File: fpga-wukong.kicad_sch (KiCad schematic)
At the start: 2 parts, among them J4 QMTECH FPGA Module U4, J5 QMTECH FPGA Module U5

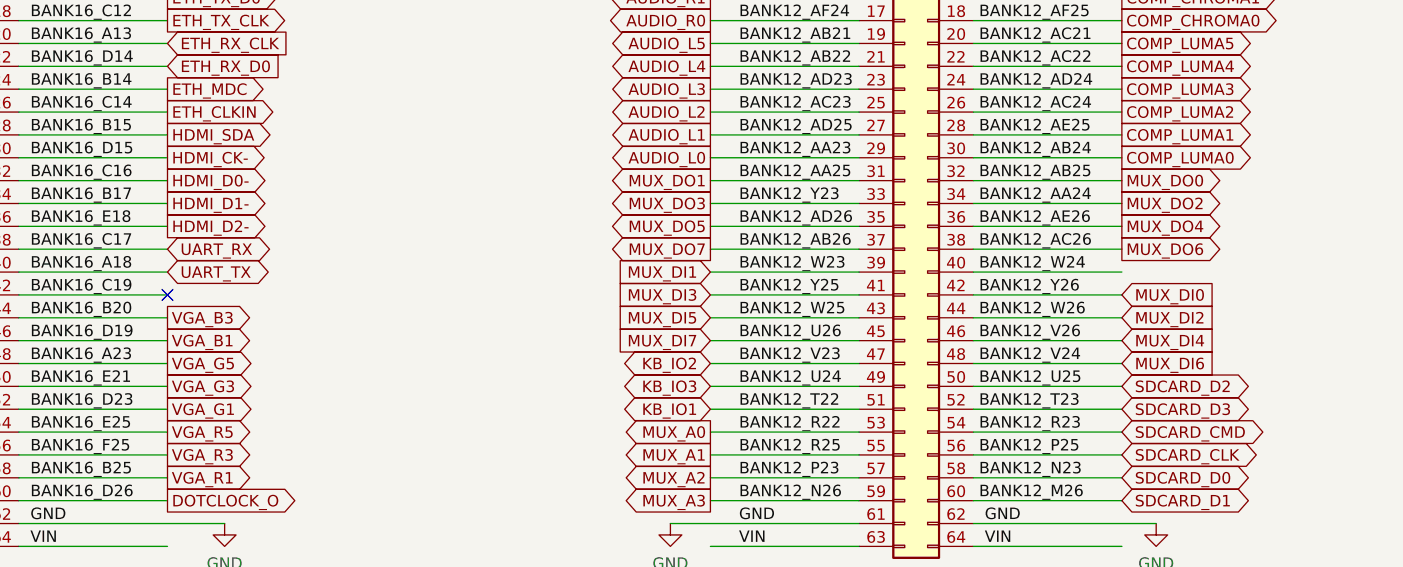
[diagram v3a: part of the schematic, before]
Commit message: switch DIP8 to DIP4 using spare pins on floppy MUX R unit
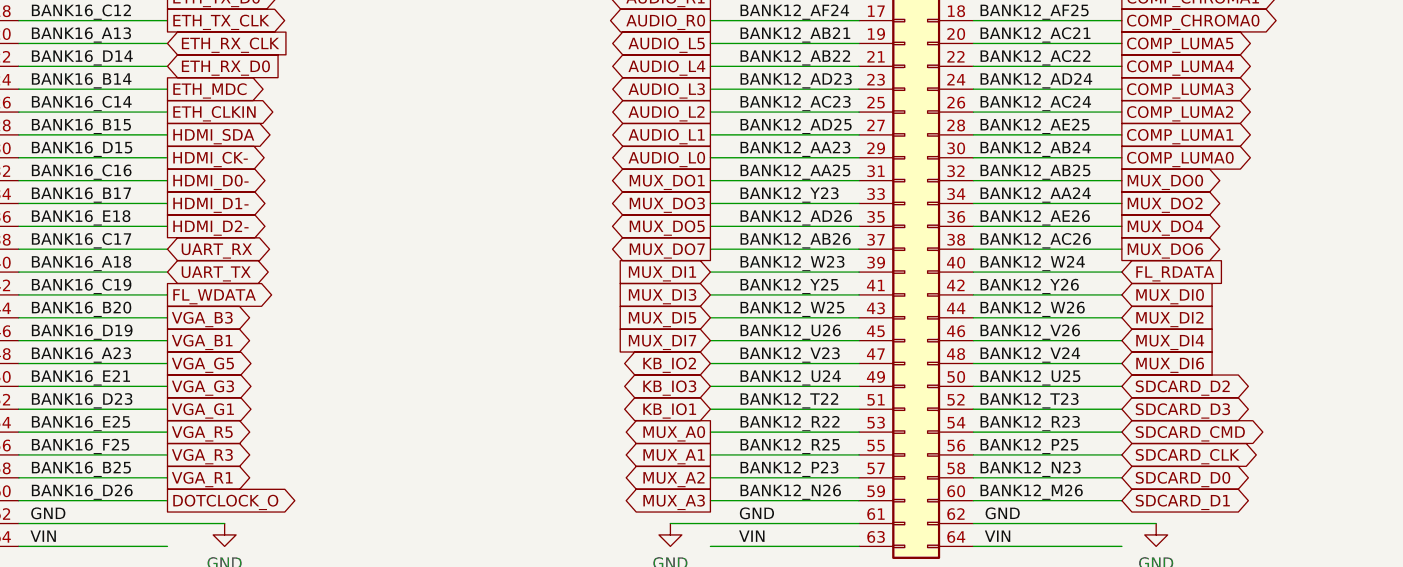
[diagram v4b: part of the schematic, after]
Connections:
- net BANK12_W24 renamed FL_RDATA
- net BANK16_C19 renamed FL_WDATA
- no-connect marks 1 -> 0
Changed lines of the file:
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@@
   (junction (at 215.265 47.625) (diameter 0) (color 0 0 0 0)
   )
-  (no_connect (at 106.045 98.425))
   (wire (pts (xy 195.58 55.245) (xy 212.09 55.245))
     (stroke (width 0) (type default) (color 0 0 0 0))
@@
     )
   )
+  (global_label "FL_RDATA" (shape input) (at 212.09 95.885 0) (fields_autoplaced)
+    (effects (font (size 1.27 1.27)) (justify left))
+    (property "Intersheet References" "${INTERSHEET_REFS}" (id 0) (at 223.2721 95.8056 0)
+      (effects (font (size 1.27 1.27)) (justify left) hide)
+    )
+  )
   (global_label "VGA_B1" (shape output) (at 106.045 103.505 0) (fields_autoplaced)
     (effects (font (size 1.27 1.27)) (justify left))
@@
       (effects (font (size 1.27 1.27)) (justify left) hide)
     )
+  )
+  (global_label "FL_WDATA" (shape output) (at 106.045 98.425 0) (fields_autoplaced)
+    (effects (font (size 1.27 1.27)) (justify left))
+    (property "Intersheet References" "${INTERSHEET_REFS}" (id 0) (at 117.4086 98.3456 0)
+      (effects (font (size 1.27 1.27)) (justify left) hide)
+    )

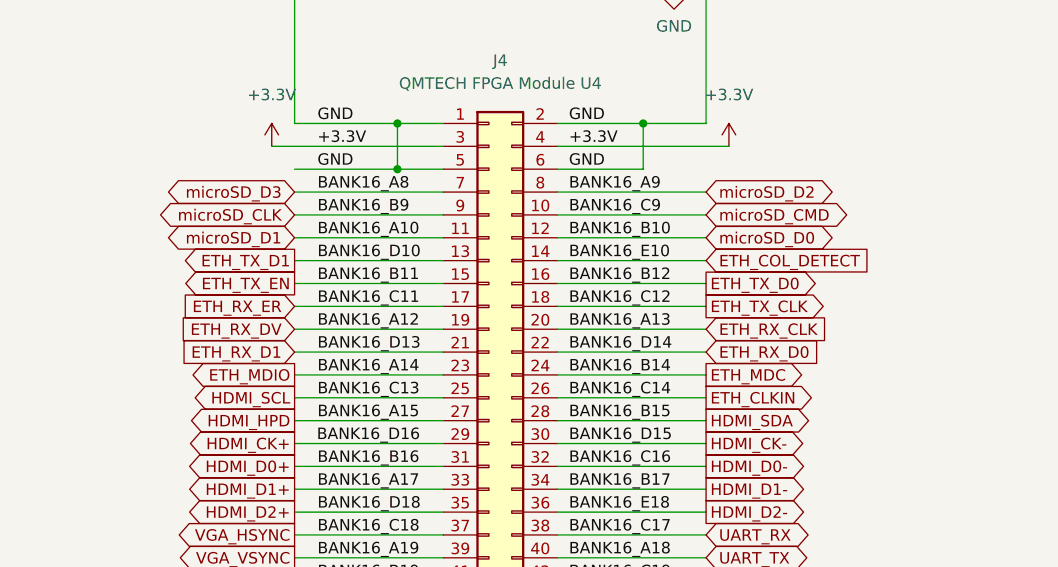
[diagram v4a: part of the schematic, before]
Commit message: relocate pins to connect RTC I2C
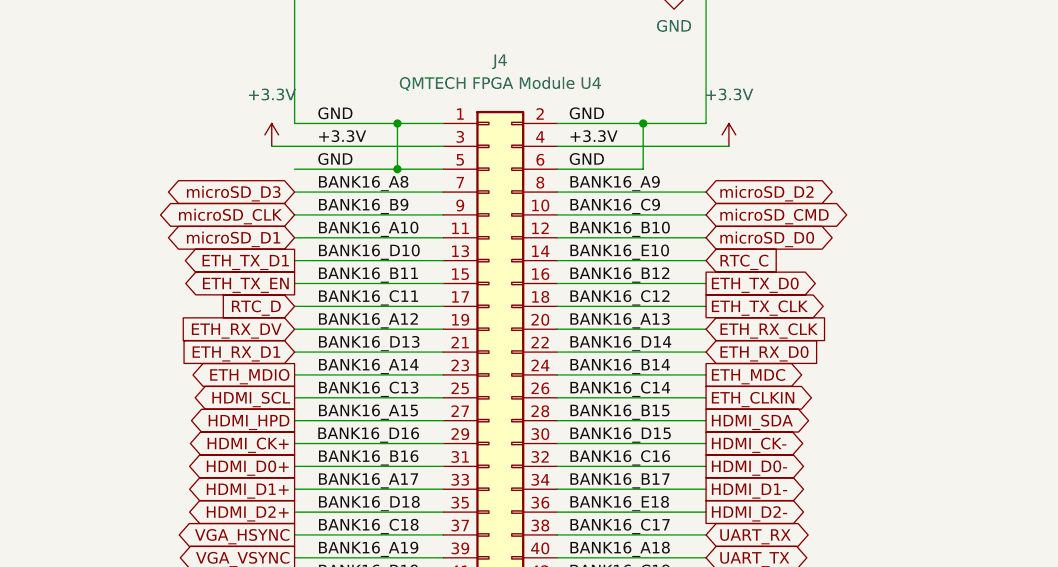
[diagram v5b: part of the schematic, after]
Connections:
- net ETH_COL_DETECT renamed RTC_C
- net ETH_RX_ER renamed RTC_D
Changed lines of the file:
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@@
+    )
+  )
+  (global_label "RTC_D" (shape input) (at 60.325 67.945 180) (fields_autoplaced)
+    (effects (font (size 1.27 1.27)) (justify right))
+    (property "Intersheet References" "${INTERSHEET_REFS}" (id 0) (at 52.1667 67.8656 0)
+      (effects (font (size 1.27 1.27)) (justify right) hide)
     )
   )
@@
     )
   )
+  (global_label "RTC_C" (shape input) (at 106.045 62.865 0) (fields_autoplaced)
+    (effects (font (size 1.27 1.27)) (justify left))
+    (property "Intersheet References" "${INTERSHEET_REFS}" (id 0) (at 114.2033 62.7856 0)
+      (effects (font (size 1.27 1.27)) (justify left) hide)
+    )
+  )
   (global_label "VGA_B1" (shape output) (at 106.045 103.505 0) (fields_autoplaced)
     (effects (font (size 1.27 1.27)) (justify left))
@@
     )
   )
-  (global_label "ETH_RX_ER" (shape input) (at 60.325 67.945 180) (fields_autoplaced)
-    (effects (font (size 1.27 1.27)) (justify right))
-    (property "Intersheet References" "${INTERSHEET_REFS}" (id 0) (at 47.6309 67.8656 0)
-      (effects (font (size 1.27 1.27)) (justify right) hide)
-    )
-  )
   (global_label "KB_IO3" (shape bidirectional) (at 166.37 108.585 180) (fields_autoplaced)
     (effects (font (size 1.27 1.27)) (justify right))
@@
       (effects (font (size 1.27 1.27)) (justify left) hide)
     )
-  )
-  (global_label "ETH_COL_DETECT" (shape input) (at 106.045 62.865 0) (fields_autoplaced)
-    (effects (font (size 1.27 1.27)) (justify left))
-    (property "Intersheet References" "${INTERSHEET_REFS}" (id 0) (at 124.2424 62.7856 0)
-      (effects (font (size 1.27 1.27)) (justify left) hide)
-    )

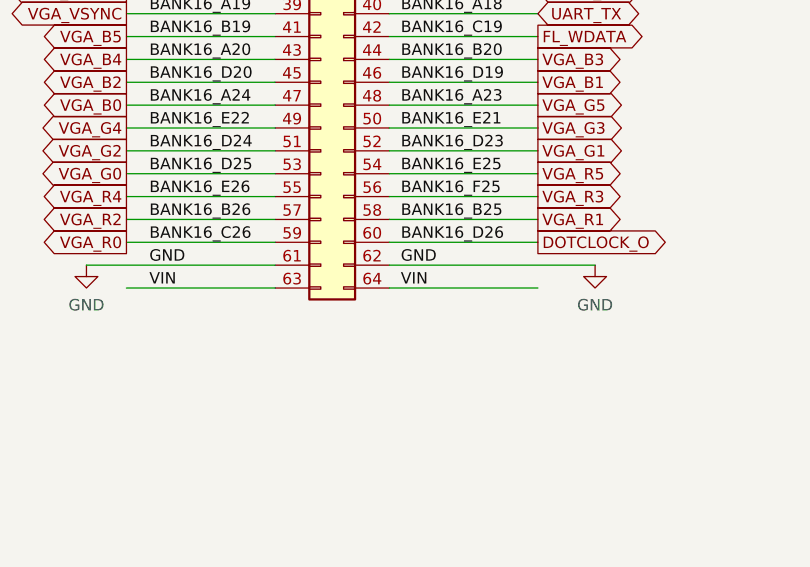
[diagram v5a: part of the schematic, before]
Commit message: try to fix B.silk, add VIN to +12V_FUSED jumper
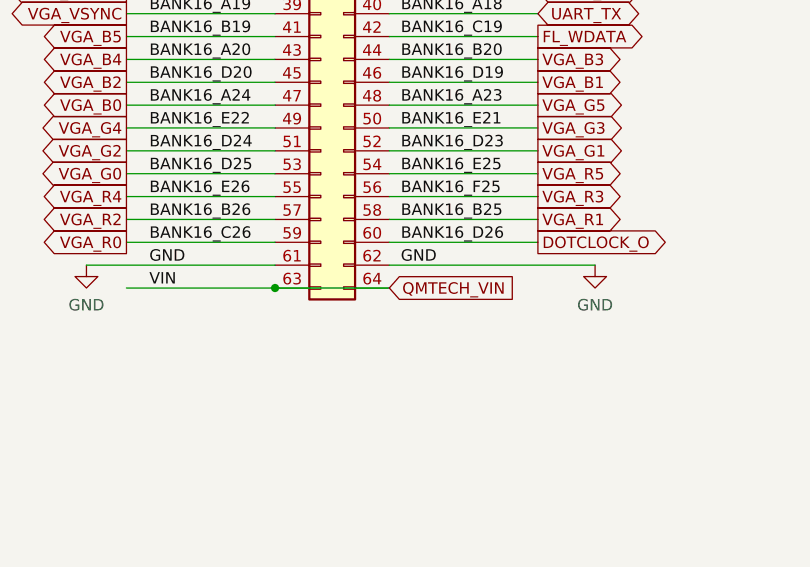
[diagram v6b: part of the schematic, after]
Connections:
- net VIN renamed QMTECH_VIN
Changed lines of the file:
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@@
   (junction (at 215.265 47.625) (diameter 0) (color 0 0 0 0)
   )
+  (junction (at 76.835 126.365) (diameter 0) (color 0 0 0 0)
+  )
   (wire (pts (xy 195.58 55.245) (xy 212.09 55.245))
     (stroke (width 0) (type default) (color 0 0 0 0))
@@
     (stroke (width 0) (type default) (color 0 0 0 0))
   )
-  (wire (pts (xy 89.535 126.365) (xy 106.045 126.365))
-    (stroke (width 0) (type default) (color 0 0 0 0))
-  )
   (wire (pts (xy 60.325 106.045) (xy 76.835 106.045))
     (stroke (width 0) (type default) (color 0 0 0 0))
@@
   )
   (wire (pts (xy 60.325 108.585) (xy 76.835 108.585))
+    (stroke (width 0) (type default) (color 0 0 0 0))
+  )
+  (wire (pts (xy 76.835 126.365) (xy 89.535 126.365))
     (stroke (width 0) (type default) (color 0 0 0 0))
   )
@@
     (effects (font (size 1.27 1.27)) (justify left bottom))
   )
-  (label "VIN" (at 90.805 126.365 0)
-    (effects (font (size 1.27 1.27)) (justify left bottom))
-  )
   (label "BANK12_W24" (at 196.215 95.885 0)
     (effects (font (size 1.27 1.27)) (justify left bottom))
@@
     )
   )
+  (global_label "QMTECH_VIN" (shape input) (at 89.535 126.365 0) (fields_autoplaced)
+    (effects (font (size 1.27 1.27)) (justify left))
+    (property "Intersheet References" "${INTERSHEET_REFS}" (id 0) (at 103.4386 126.2856 0)
+      (effects (font (size 1.27 1.27)) (justify left) hide)
+    )
+  )
